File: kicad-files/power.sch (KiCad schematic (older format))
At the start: 7 parts

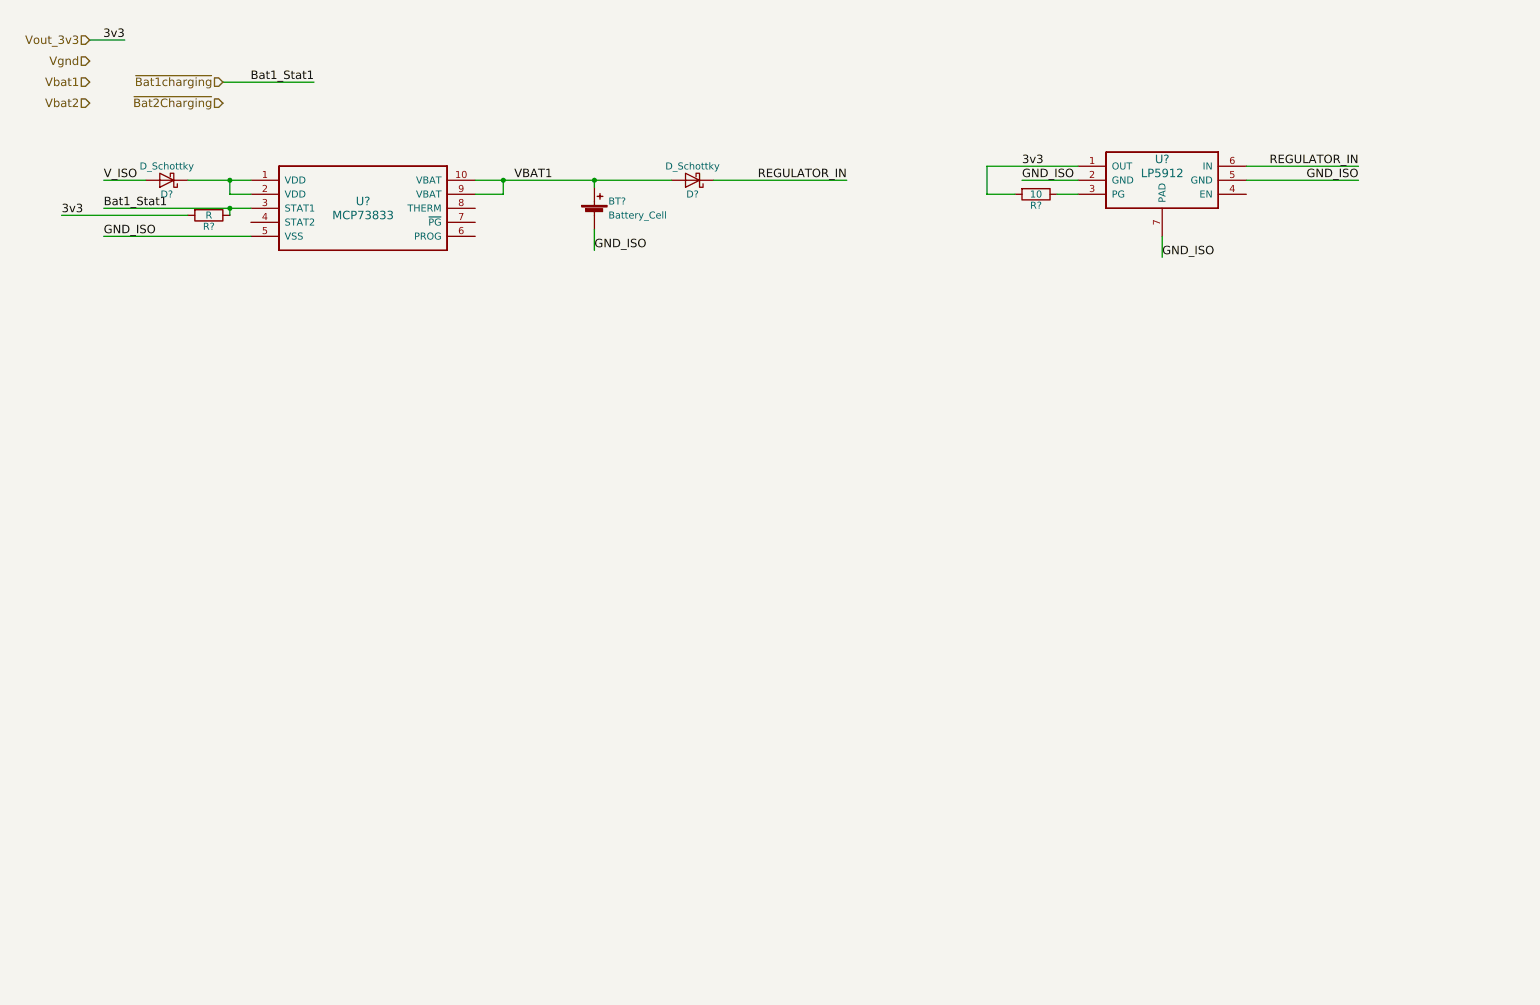
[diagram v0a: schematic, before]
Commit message: sketch-in thermister to power sheet
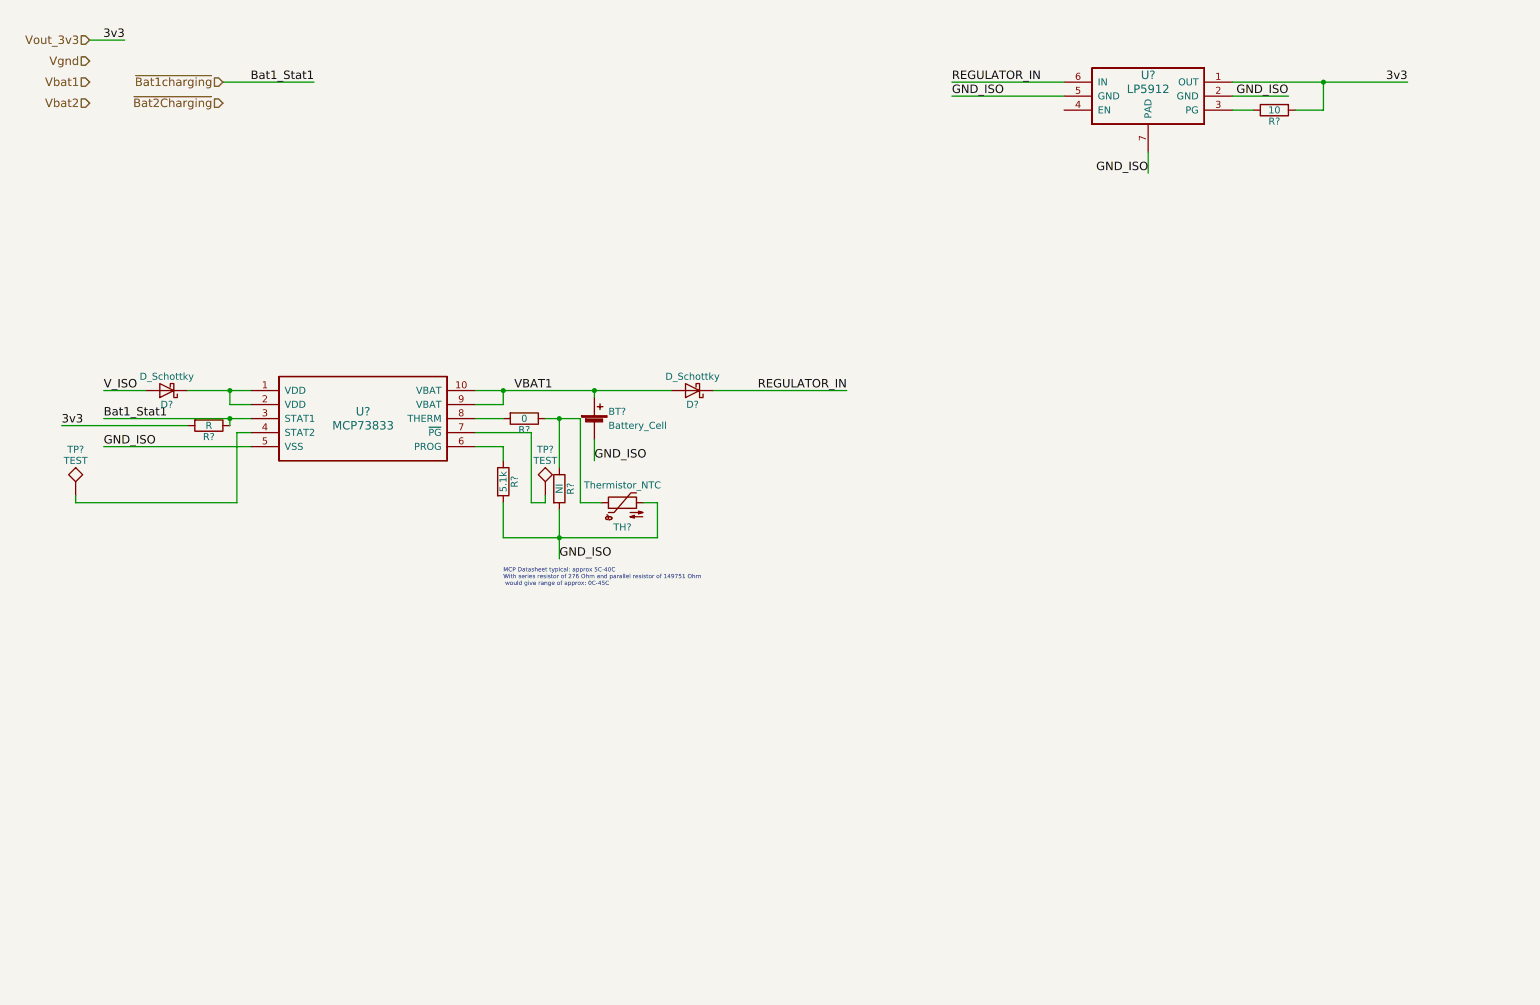
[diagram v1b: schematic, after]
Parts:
- added R?: 5.1k, symbol R
- added R?: 0, symbol R
- added R?: NI, symbol R
- added TH?: Thermistor_NTC, symbol Thermistor_NTC
- added TP? (x2): TEST, symbol TEST
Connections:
- net GND_ISO: now also R?.2, R?.2, TH?.2
- net at U?.4 (STAT2): now also TP?.1
- net at U?.6 (PROG): now also R?.1
- net at U?.7 (~PG~): now also TP?.1
- net at U?.8 (THERM): now also R?.2
- new net: R?.1, R?.1, TH?.1
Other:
- note added: "MCP Datasheet typical: approx 5C-40C\nWith series resistor of 276 Ohm and parallel resistor of 149751 Ohm\n would give range of approx: 0C-45C"
- moved on the sheet: BT?, D?, R?, U?

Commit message: added micro-USB and isolated power
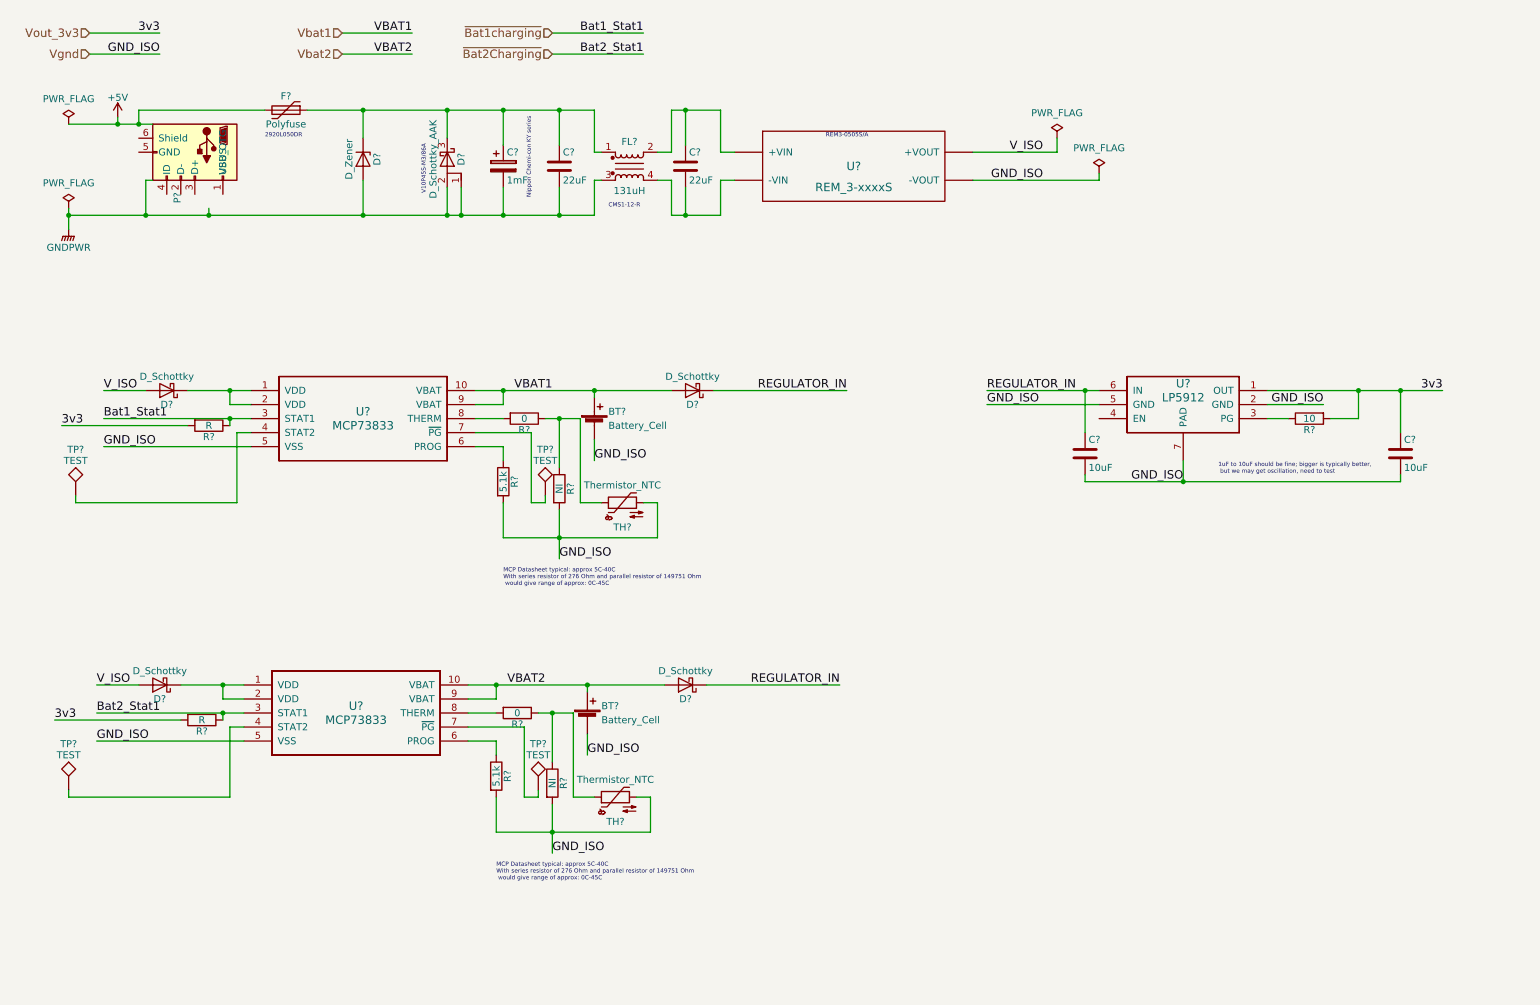
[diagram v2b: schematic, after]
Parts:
- added BT?: Battery_Cell, symbol Battery_Cell
- added C? (x2): 10uF, symbol C
- added C?: 1mF, symbol CP
- added C? (x2): 22uF, symbol C
- added D? (x2): D_Schottky, symbol D_Schottky
- added D?: D_Schottky_AAK, symbol D_Schottky_AAK
- added D?: D_Zener, symbol D_Zener
- added F?: Polyfuse, symbol Polyfuse
- added FL?: 131uH, symbol EMI_Filter_LL
- added P?: USB_OTG, symbol USB_OTG
- added R?: R, symbol R
- added R?: 5.1k, symbol R
- added R?: 0, symbol R
- added R?: NI, symbol R
- added TH?: Thermistor_NTC, symbol Thermistor_NTC
- added TP? (x2): TEST, symbol TEST
- added U?: MCP73833, symbol MCP73833
- added U?: REM_3-xxxxS, symbol REM_3-xxxxS
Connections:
- net GND_ISO is gone; now on net Vgnd: BT?.2 (-), R?.2, R?.2, TH?.2, U?.2 (GND), U?.5 (GND), U?.5 (VSS), U?.7 (PAD)
- net VBAT1 is gone; now on net Vbat1: BT?.1 (+), D?.2 (A), U?.10 (VBAT), U?.9 (VBAT)
- net REGULATOR_IN: now also C?.1, D?.1 (K)
- net V_ISO: now also D?.2 (A), U?.~ (-VOUT)
- net Vbat2: now also BT?.1 (+), D?.2 (A), U?.10 (VBAT), U?.9 (VBAT)
- net Vgnd: now also BT?.2 (-), C?.2, C?.2, R?.2, R?.2, TH?.2, U?.5 (VSS), U?.~ (-VOUT)
- net Vout_3v3: now also C?.1, R?.2
- net ~Bat2Charging~: now also R?.1, U?.3 (STAT1)
- new net: D?.1 (K), U?.1 (VDD), U?.2 (VDD)
- new net: TP?.1, U?.4 (STAT2)
- new net: R?.1, U?.6 (PROG)
- new net: TP?.1, U?.7 (~PG~)
- new net: R?.2, U?.8 (THERM)
- new net: R?.1, R?.1, TH?.1
- new net: C?.1, FL?.2, U?.~ (-VOUT)
- new net: C?.2, FL?.4, U?.~ (-VOUT)
- new net: C?.1, C?.1, D?.1 (K), D?.3 (K), F?.1, FL?.1
- new net +5V: F?.2
- new net GNDPWR: C?.2, C?.2, D?.1 (A), D?.2 (A), D?.2 (A), FL?.3
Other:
- note added: "1uF to 10uF should be fine; bigger is typically better,\n but we may get oscillation, need to test"
- note added: "2920L050DR"
- note added: "CMS1-12-R"
- note added: "Nippon Chemi-con KY series"
- note added: "REM3-0505S/A"
- note added: "V10P45S-M3/86A"
- moved on the sheet: R?, U?

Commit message: schematic first draft
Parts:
- added SW?: SW_Push_Open, symbol SW_Push_Open
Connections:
- net REGULATOR_IN: now also SW?.1 (A); no longer C?.1, U?.6 (IN)
- net V_ISO renamed FTDI_V_ISO
- new net: C?.1, SW?.2 (B), U?.6 (IN)
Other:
- note added: "TODO: Add USB-C also"
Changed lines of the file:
@@
 LIBS:lp5912
 LIBS:rem_3-xxxxs
+LIBS:switches
 LIBS:OpenHardwareHolterMonitor-cache
 EELAYER 25 0
@@
 Text Label 1150 3600 0    60   ~ 0
 GND_ISO
-Text Label 4350 3200 2    60   ~ 0
+Text Label 4900 3200 2    60   ~ 0
 VBAT1
 Text HLabel 4350 650  0    60   Input ~ 0
@@
 	-1   0    0    -1
 $EndComp
-Text Label 7450 3200 0    60   ~ 0
+Text Label 6800 3200 0    60   ~ 0
 REGULATOR_IN
 Text Label 6450 3200 2    60   ~ 0
 REGULATOR_IN
-Text Label 7450 3300 0    60   ~ 0
+Text Label 6800 3300 0    60   ~ 0
 GND_ISO
 Text Label 10700 3200 2    60   ~ 0
@@
 Text Label 1100 5700 0    60   ~ 0
 GND_ISO
-Text Label 4300 5300 2    60   ~ 0
+Text Label 4850 5300 2    60   ~ 0
 VBAT2
 Text Label 1100 5500 0    60   ~ 0
@@
 Connection ~ 4650 3200
 Wire Wire Line
-	7450 3200 8250 3200
+	8000 3200 8250 3200
 Wire Wire Line
 	5500 3200 6450 3200
 Wire Wire Line
-	8250 3300 7450 3300
+	8250 3300 6800 3300
 Wire Wire Line
 	9450 3200 10700 3200
@@
 Wire Wire Line
 	8250 1700 8250 1650
+Wire Wire Line
+	7600 3200 6800 3200
+$Comp
+L SW_Push_Open SW?
+U 1 1 5AB77FDE
+P 7800 3200
+F 0 "SW?" H 7800 3300 50  0000 C CNN
+F 1 "SW_Push_Open" H 7800 3125 50  0000 C CNN
+F 2 "" H 7800 3400 50  0000 C CNN
+F 3 "" H 7800 3400 50  0000 C CNN
+	1    7800 3200
+	1    0    0    -1
+$EndComp
+Text HLabel 5800 650  0    60   Input ~ 0
+FTDI_V_ISO
+Wire Wire Line
+	5800 650  6300 650
+Text Label 6300 650  2    60   ~ 0
+V_ISO
+Text Notes 1300 2250 0    60   ~ 0
+TODO: Add USB-C also
 $EndSCHEMATC

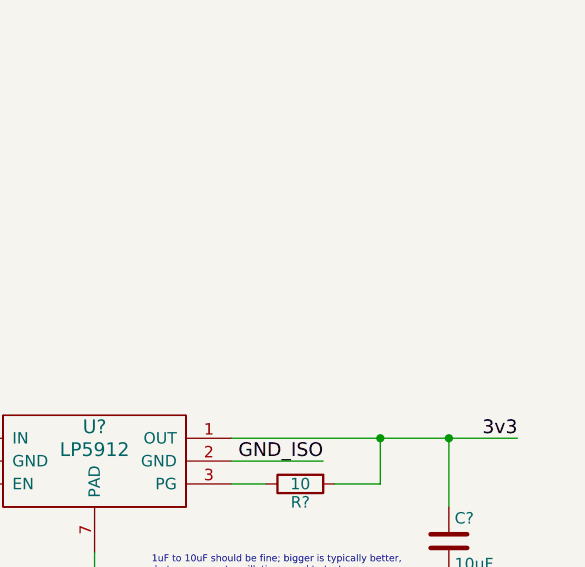
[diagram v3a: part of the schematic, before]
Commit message: add vbat to header, and optional power LED
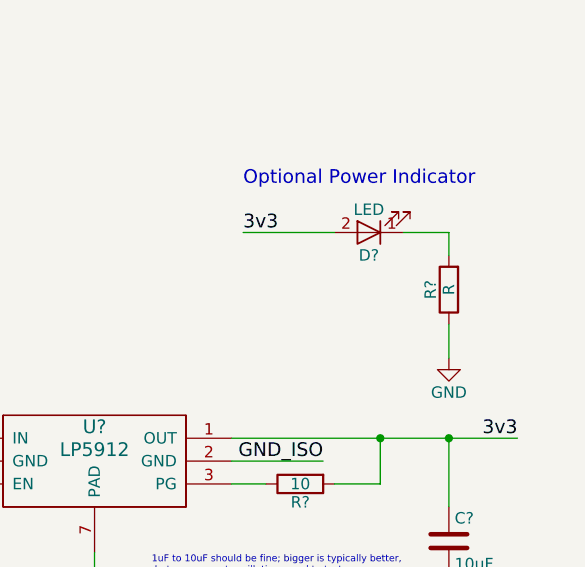
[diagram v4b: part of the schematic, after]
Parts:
- added D?: LED, symbol LED
- added R?: R, symbol R
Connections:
- net Vout_3v3: now also D?.2 (A)
- new net: D?.1 (K), R?.2
- new net GND: R?.1
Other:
- note added: "Optional Power Indicator"
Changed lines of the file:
@@
 Text Notes 1300 2250 0    60   ~ 0
 TODO: Add USB-C also
+$Comp
+L LED D?
+U 1 1 5AB70007
+P 10050 2300
+F 0 "D?" H 10050 2400 50  0000 C CNN
+F 1 "LED" H 10050 2200 50  0000 C CNN
+F 2 "" H 10050 2300 50  0000 C CNN
+F 3 "" H 10050 2300 50  0000 C CNN
+	1    10050 2300
+	-1   0    0    1
+$EndComp
+$Comp
+L R R?
+U 1 1 5AB7020A
+P 10400 2550
+F 0 "R?" V 10480 2550 50  0000 C CNN
+F 1 "R" V 10400 2550 50  0000 C CNN
+F 2 "" V 10330 2550 50  0000 C CNN
+F 3 "" H 10400 2550 50  0000 C CNN
+	1    10400 2550
+	-1   0    0    1
+$EndComp
+$Comp
+L GND #PWR?
+U 1 1 5AB7048D
+P 10400 2850
+F 0 "#PWR?" H 10400 2600 50  0001 C CNN
+F 1 "GND" H 10400 2700 50  0000 C CNN
+F 2 "" H 10400 2850 50  0000 C CNN
+F 3 "" H 10400 2850 50  0000 C CNN
+	1    10400 2850
+	1    0    0    -1
+$EndComp
+Wire Wire Line
+	9500 2300 9900 2300
+Wire Wire Line
+	10200 2300 10400 2300
+Wire Wire Line
+	10400 2300 10400 2400
+Wire Wire Line
+	10400 2700 10400 2850
+Text Label 9500 2300 0    60   ~ 0
+3v3
+Text Notes 9500 2100 0    60   ~ 0
+Optional Power Indicator
 $EndSCHEMATC

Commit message: kicad-4.0.7
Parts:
- removed P?: USB_OTG, symbol USB_OTG
- added J?: USB_OTG, symbol USB_OTG
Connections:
- net +5V: now also J?.1 (VBUS)
- net GNDPWR: now also J?.5 (GND), J?.6 (Shield)
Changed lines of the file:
@@
 EESchema Schematic File Version 2
+LIBS:OpenHardwareHolterMonitor-rescue
 LIBS:power
 LIBS:device
@@
 VBAT2
 $Comp
-L USB_OTG P?
-U 1 1 5AAD4608
-P 1800 1500
-F 0 "P?" H 2125 1375 50  0000 C CNN
-F 1 "USB_OTG" H 1800 1700 50  0000 C CNN
-F 2 "" V 1750 1400 50  0000 C CNN
-F 3 "" V 1750 1400 50  0000 C CNN
-	1    1800 1500
-	0    1    1    0
-$EndComp
-$Comp
 L GNDPWR #PWR?
 U 1 1 5AAD4720
@@
 	900  1950 4650 1950
 Wire Wire Line
-	1450 1950 1450 1700
-Wire Wire Line
-	1450 1700 1500 1700
-Wire Wire Line
 	900  1300 1500 1300
 Wire Wire Line
 	1250 1300 1250 1250
 Connection ~ 1250 1300
-Connection ~ 1450 1950
 Wire Wire Line
 	1900 1950 1900 1900
@@
 Text Notes 9500 2100 0    60   ~ 0
 Optional Power Indicator
+$Comp
+L USB_OTG J?
+U 1 1 5AD33DB1
+P 1800 1500
+F 0 "J?" H 1600 1950 50  0000 L CNN
+F 1 "USB_OTG" H 1600 1850 50  0000 L CNN
+F 2 "" H 1950 1450 50  0001 C CNN
+F 3 "" H 1950 1450 50  0001 C CNN
+	1    1800 1500
+	-1   0    0    -1
+$EndComp
+Wire Wire Line
+	1800 1900 1800 1950
+Connection ~ 1800 1950
 $EndSCHEMATC
